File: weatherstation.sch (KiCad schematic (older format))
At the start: 0 parts

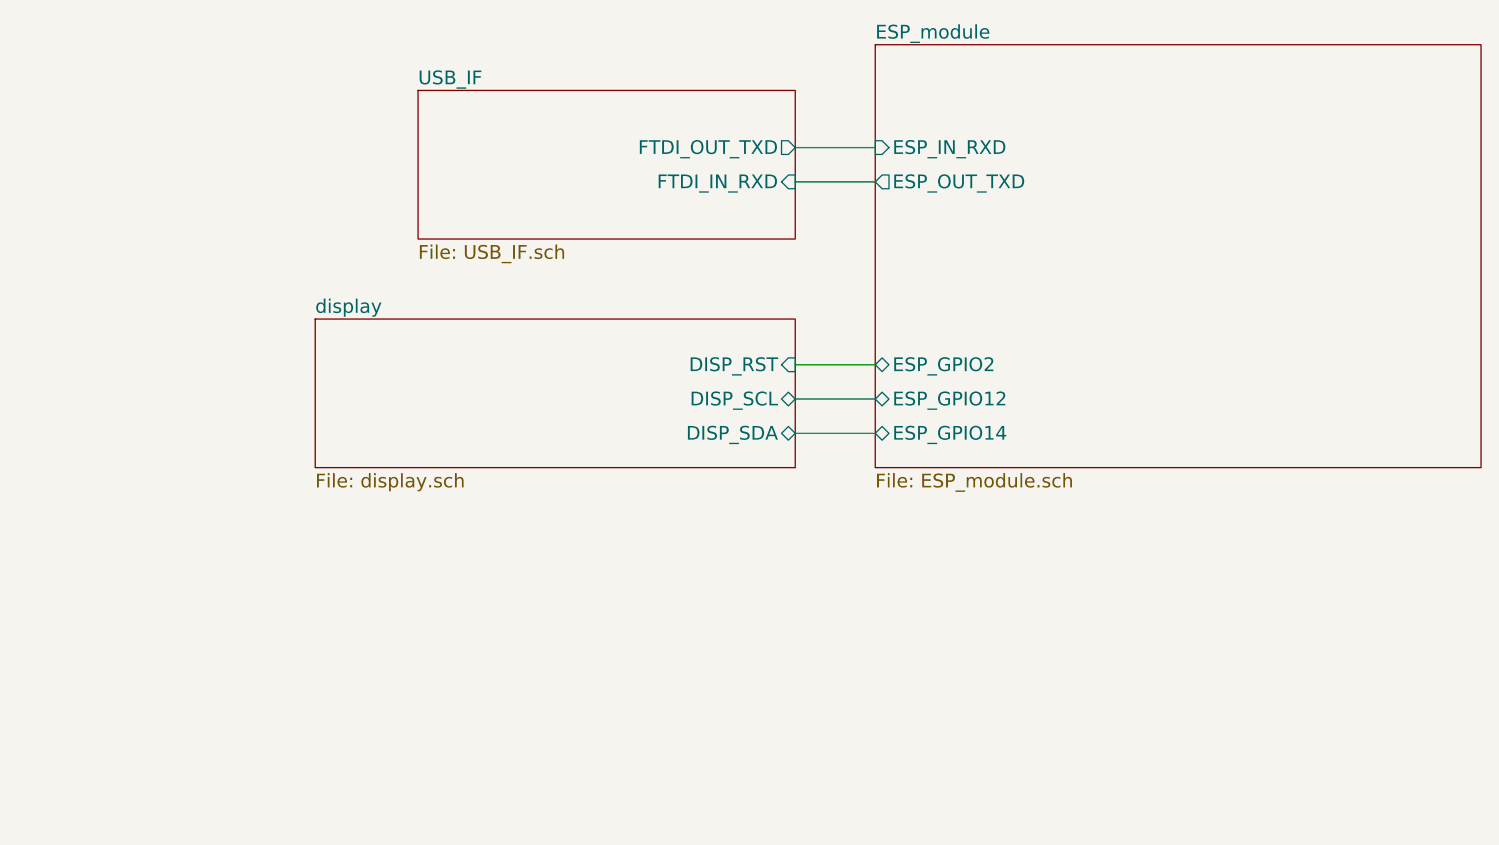
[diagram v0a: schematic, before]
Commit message: Started adding component values and tidying up
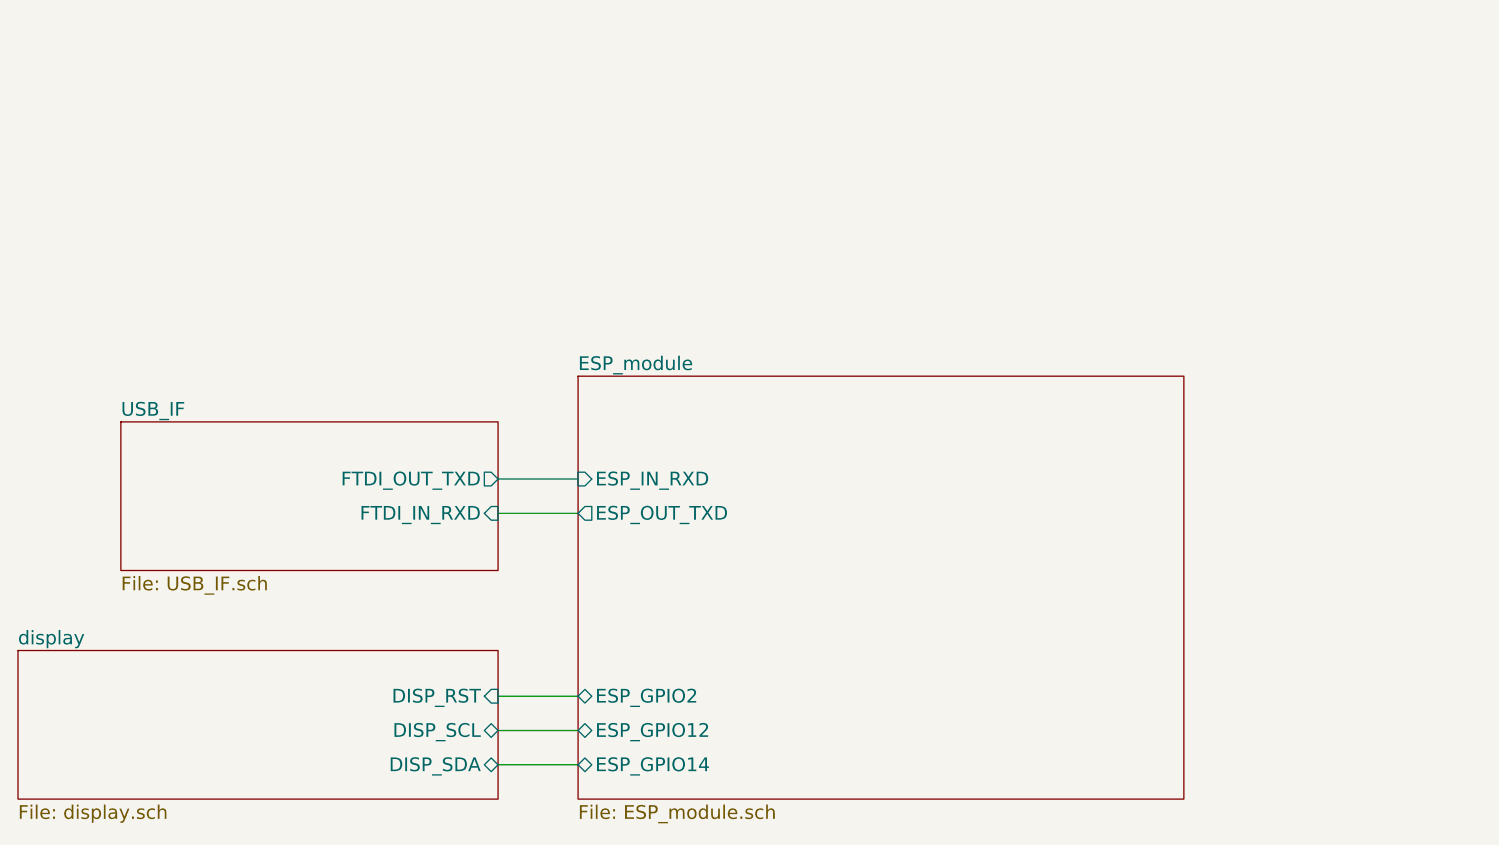
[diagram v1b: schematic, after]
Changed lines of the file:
@@
 $EndDescr
 $Sheet
-S 5200 1850 1650 650
+S 3900 3300 1650 650
 U 563FE165
 F0 "USB_IF" 60
 F1 "USB_IF.sch" 60
-F2 "FTDI_OUT_TXD" O R 6850 2100 60
-F3 "FTDI_IN_RXD" I R 6850 2250 60
+F2 "FTDI_OUT_TXD" O R 5550 3550 60
+F3 "FTDI_IN_RXD" I R 5550 3700 60
 $EndSheet
 $Sheet
-S 7200 1650 2650 1850
+S 5900 3100 2650 1850
 U 564003DD
 F0 "ESP_module" 60
 F1 "ESP_module.sch" 60
-F2 "ESP_GPIO2" B L 7200 3050 60
-F3 "ESP_GPIO12" B L 7200 3200 60
-F4 "ESP_GPIO14" B L 7200 3350 60
-F5 "ESP_IN_RXD" I L 7200 2100 60
-F6 "ESP_OUT_TXD" O L 7200 2250 60
+F2 "ESP_GPIO2" B L 5900 4500 60
+F3 "ESP_GPIO12" B L 5900 4650 60
+F4 "ESP_GPIO14" B L 5900 4800 60
+F5 "ESP_IN_RXD" I L 5900 3550 60
+F6 "ESP_OUT_TXD" O L 5900 3700 60
 $EndSheet
 $Sheet
-S 4750 2850 2100 650
+S 3450 4300 2100 650
 U 564032BC
 F0 "display" 60
 F1 "display.sch" 60
-F2 "DISP_SCL" T R 6850 3200 60
-F3 "DISP_SDA" T R 6850 3350 60
-F4 "DISP_RST" I R 6850 3050 60
+F2 "DISP_SCL" T R 5550 4650 60
+F3 "DISP_SDA" T R 5550 4800 60
+F4 "DISP_RST" I R 5550 4500 60
 $EndSheet
 Wire Wire Line
-	7200 3050 6850 3050
+	5900 4500 5550 4500
 Wire Wire Line
-	6850 3200 7200 3200
+	5550 4650 5900 4650
 Wire Wire Line
-	7200 3350 6850 3350
+	5900 4800 5550 4800
 Wire Wire Line
-	7200 2250 6850 2250
+	5900 3700 5550 3700
 Wire Wire Line
-	7200 2100 6850 2100
+	5900 3550 5550 3550
 $EndSCHEMATC
